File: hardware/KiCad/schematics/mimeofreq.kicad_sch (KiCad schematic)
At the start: 19 parts, among them J1 AudioJack2, J2 AudioJack2, J3 Barrel_Jack_Switch_Pin3Ring, SW1 SW_SPST, SW2 SW_SPST, SW3 SW_SPDT

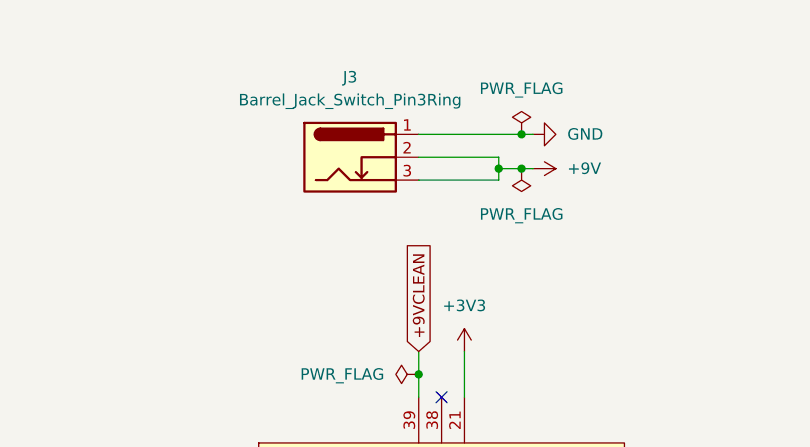
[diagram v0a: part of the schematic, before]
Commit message: Adding op amps to board; bypass cap correction.
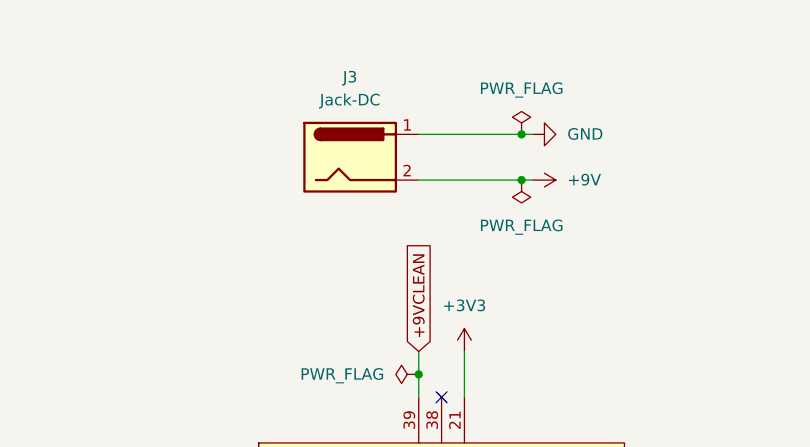
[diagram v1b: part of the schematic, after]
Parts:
- removed J3: Barrel_Jack_Switch_Pin3Ring, Connector_Wire_Custom:SolderWire-0.5sqmm_1x03_P4.6mm_D0.9mm_OD2.1mm_BarrelJack, symbol Connector:Barrel_Jack_Switch_Pin3Ring
- added J3: Jack-DC, Connector_Wire:SolderWire-0.5sqmm_1x02_P4.6mm_D0.9mm_OD2.1mm, symbol Connector:Jack-DC
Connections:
- net +9V: now also J3.2
- net GND: now also J3.1
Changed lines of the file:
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@@
 	)
 	(junction
-		(at 238.76 40.64)
+		(at 238.76 41.91)
 		(diameter 0)
 		(color 0 0 0 0)
@@
 	)
 	(junction
-		(at 236.22 40.64)
-		(diameter 0)
-		(color 0 0 0 0)
-	)
-	(junction
 		(at 135.89 62.23)
 		(diameter 0)
@@
 	(wire
 		(pts
+			(xy 227.33 41.91) (xy 240.03 41.91)
+		)
+		(stroke
+			(width 0)
+			(type default)
+		)
+	)
+	(wire
+		(pts
 			(xy 135.89 62.23) (xy 135.89 66.04)
 		)
@@
 	(wire
 		(pts
-			(xy 236.22 39.37) (xy 236.22 40.64)
-		)
-		(stroke
-			(width 0)
-			(type default)
-		)
-	)
-	(wire
-		(pts
 			(xy 69.85 142.24) (xy 86.36 142.24)
 		)
@@
 	(wire
 		(pts
-			(xy 236.22 40.64) (xy 236.22 41.91)
-		)
-		(stroke
-			(width 0)
-			(type default)
-		)
-	)
-	(wire
-		(pts
 			(xy 62.23 179.07) (xy 66.04 179.07)
 		)
@@
 	(wire
 		(pts
-			(xy 236.22 40.64) (xy 240.03 40.64)
-		)
-		(stroke
-			(width 0)
-			(type default)
-		)
-	)
-	(wire
-		(pts
 			(xy 73.66 179.07) (xy 77.47 179.07)
 		)
@@
 	(wire
 		(pts
-			(xy 236.22 41.91) (xy 227.33 41.91)
-		)
-		(stroke
-			(width 0)
-			(type default)
-		)
-	)
-	(wire
-		(pts
 			(xy 66.04 130.81) (xy 86.36 130.81)
 		)
@@
 		(pts
 			(xy 86.36 153.67) (xy 86.36 165.1)
-		)
-		(stroke
-			(width 0)
-			(type default)
-		)
-	)
-	(wire
-		(pts
-			(xy 227.33 39.37) (xy 236.22 39.37)
 		)
 		(stroke
@@
 	(symbol
 		(lib_id "power:+9V")
-		(at 240.03 40.64 270)
+		(at 240.03 41.91 270)
 		(unit 1)
 		(body_style 1)
@@
 		(fields_autoplaced yes)
 		(property "Reference" "#PWR018"
-			(at 236.22 40.64 0)
+			(at 236.22 41.91 0)
 			(hide yes)
 			(show_name no)
@@
 		)
 		(property "Value" "+9V"
-			(at 243.84 40.6399 90)
+			(at 243.84 41.9099 90)
 			(show_name no)
 			(do_not_autoplace no)
@@
 		)
 		(property "Footprint" ""
-			(at 240.03 40.64 0)
+			(at 240.03 41.91 0)
 			(hide yes)
 			(show_name no)
@@
 		)
 		(property "Datasheet" ""
-			(at 240.03 40.64 0)
+			(at 240.03 41.91 0)
 			(hide yes)
 			(show_name no)
@@
 		)
 		(property "Description" "Power symbol creates a global label with name \"+9V\""
-			(at 240.03 40.64 0)
+			(at 240.03 41.91 0)
 			(hide yes)
 			(show_name no)
@@
 	)
 	(symbol
-		(lib_id "Connector:Barrel_Jack_Switch_Pin3Ring")
-		(at 219.71 39.37 0)
-		(unit 1)
-		(body_style 1)
-		(exclude_from_sim no)
-		(in_bom yes)
-		(on_board yes)
-		(in_pos_files yes)
-		(dnp no)
-		(fields_autoplaced yes)
-		(property "Reference" "J3"
-			(at 219.71 30.48 0)
-			(show_name no)
-			(do_not_autoplace no)
-			(effects
-				(font
-					(size 1.27 1.27)
-				)
-			)
-		)
-		(property "Value" "Barrel_Jack_Switch_Pin3Ring"
-			(at 219.71 33.02 0)
-			(show_name no)
-			(do_not_autoplace no)
-			(effects
-				(font
-					(size 1.27 1.27)
-				)
-			)
-		)
-		(property "Footprint" "Connector_Wire_Custom:SolderWire-0.5sqmm_1x03_P4.6mm_D0.9mm_OD2.1mm_BarrelJack"
-			(at 220.98 40.386 0)
-			(hide yes)
-			(show_name no)
-			(do_not_autoplace no)
-			(effects
-				(font
-					(size 1.27 1.27)
-				)
-			)
-		)
-		(property "Datasheet" ""
-			(at 220.98 40.386 0)
-			(hide yes)
-			(show_name no)
-			(do_not_autoplace no)
-			(effects
-				(font
-					(size 1.27 1.27)
-				)
-			)
-		)
-		(property "Description" "DC Barrel Jack with an internal switch"
-			(at 219.71 39.37 0)
-			(hide yes)
-			(show_name no)
-			(do_not_autoplace no)
-			(effects
-				(font
-					(size 1.27 1.27)
-				)
-			)
-		)
-		(pin "1"
-		)
-		(pin "3"
-		)
-		(pin "2"
-		)
-		(instances
-			(project "mimeofreq"
-				(path "/fc444d3c-3a1a-4715-bcff-119f4d2b4d9e"
-					(reference "J3")
-					(unit 1)
-				)
-			)
-		)
-	)
-	(symbol
 		(lib_id "Device:LED")
 		(at 133.35 138.43 0)
@@
 	(symbol
 		(lib_id "power:PWR_FLAG")
-		(at 238.76 40.64 180)
+		(at 238.76 41.91 180)
 		(unit 1)
 		(body_style 1)
@@
 		(fields_autoplaced yes)
 		(property "Reference" "#FLG03"
-			(at 238.76 42.545 0)
+			(at 238.76 43.815 0)
 			(hide yes)
 			(show_name no)
@@
 		)
 		(property "Value" "PWR_FLAG"
-			(at 238.76 45.72 0)
+			(at 238.76 46.99 0)
 			(show_name no)
 			(do_not_autoplace no)
@@
 		)
 		(property "Footprint" ""
-			(at 238.76 40.64 0)
+			(at 238.76 41.91 0)
 			(hide yes)
 			(show_name no)
@@
 		)
 		(property "Datasheet" ""
-			(at 238.76 40.64 0)
+			(at 238.76 41.91 0)
 			(hide yes)
 			(show_name no)
@@
 		)
 		(property "Description" "Special symbol for telling ERC where power comes from"
-			(at 238.76 40.64 0)
+			(at 238.76 41.91 0)
 			(hide yes)
 			(show_name no)
@@
 					(unit 1)
 				)
+			)
+		)
+	)
+	(symbol
+		(lib_id "Connector:Jack-DC")
+		(at 219.71 39.37 0)
+		(unit 1)
+		(body_style 1)
+		(exclude_from_sim no)
+		(in_bom yes)
+		(on_board yes)
+		(in_pos_files yes)
+		(dnp no)
+		(fields_autoplaced yes)
+		(property "Reference" "J3"
+			(at 219.71 30.48 0)
+			(show_name no)
+			(do_not_autoplace no)
+			(effects
+				(font
+					(size 1.27 1.27)
+				)
+			)
+		)
+		(property "Value" "Jack-DC"
+			(at 219.71 33.02 0)
+			(show_name no)
+			(do_not_autoplace no)
+			(effects
+				(font
+					(size 1.27 1.27)
+				)
+			)
+		)
+		(property "Footprint" "Connector_Wire:SolderWire-0.5sqmm_1x02_P4.6mm_D0.9mm_OD2.1mm"
+			(at 220.98 40.386 0)
+			(hide yes)
+			(show_name no)
+			(do_not_autoplace no)
+			(effects
+				(font
+					(size 1.27 1.27)
+				)
+			)
+		)
+		(property "Datasheet" ""
+			(at 220.98 40.386 0)
+			(hide yes)
+			(show_name no)
+			(do_not_autoplace no)
+			(effects
+				(font
+					(size 1.27 1.27)
+				)
+			)
+		)
+		(property "Description" "DC Barrel Jack"
+			(at 219.71 39.37 0)
+			(hide yes)
+			(show_name no)
+			(do_not_autoplace no)
+			(effects
+				(font
+					(size 1.27 1.27)
+				)
+			)
+		)
+		(pin "2"
+		)
+		(pin "1"
+		)
+		(instances
+			(project "mimeofreq"
+				(path "/fc444d3c-3a1a-4715-bcff-119f4d2b4d9e"
+					(reference "J3")
+					(unit 1)
+				)
